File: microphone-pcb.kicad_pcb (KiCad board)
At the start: 4 copper layers, 10.7 x 11 mm, 13 parts, among them J1 Conn_FFC_Molex_5019510550

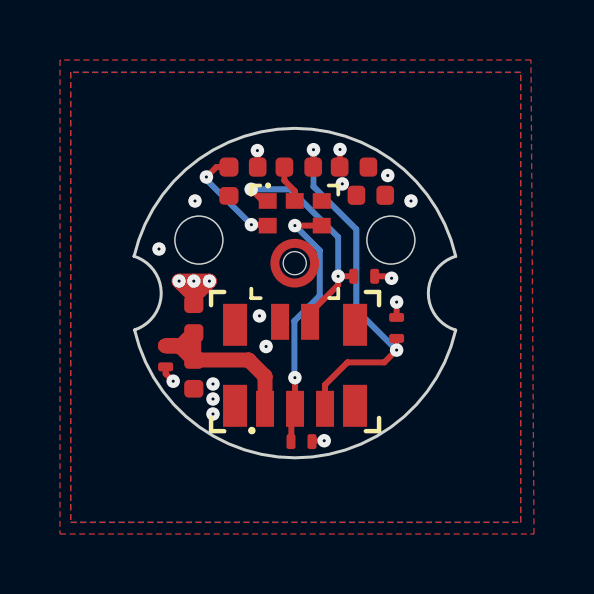
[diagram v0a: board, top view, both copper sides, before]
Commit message: [#71986] Update zones clearance
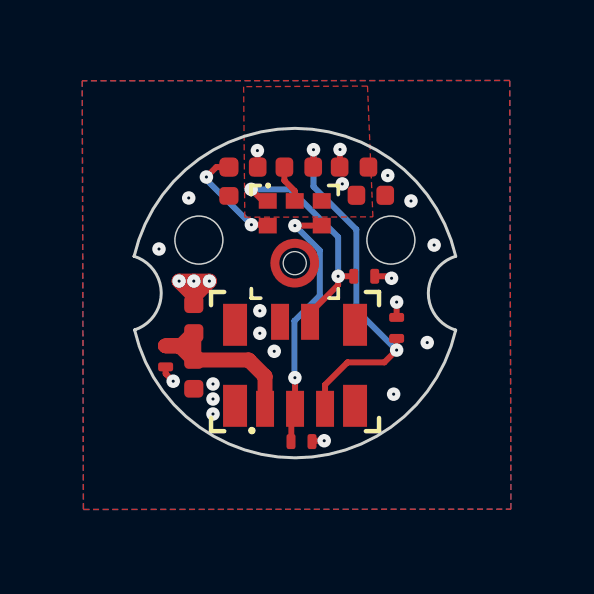
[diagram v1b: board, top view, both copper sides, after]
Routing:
- net GND: vias 13 -> 17
- added copper zone on In2.Cu, net GND

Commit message: [#71986] Update Silk L/R channels
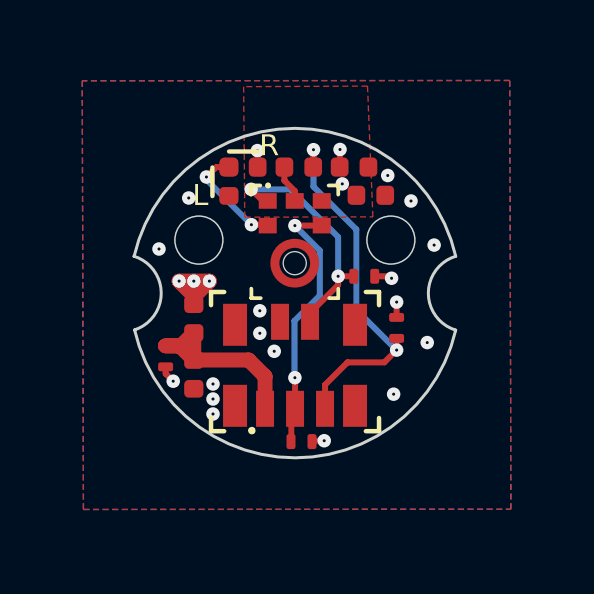
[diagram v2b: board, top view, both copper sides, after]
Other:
- board text added: "L"
- board text added: "R"
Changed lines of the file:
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@@
+	)
+	(gr_line
+		(start 238.7312 142.1966)
+		(end 237.7812 142.1966)
+		(stroke
+			(width 0.15)
+			(type default)
+		)
+		(layer "F.SilkS")
+	)
+	(gr_line
+		(start 237.2262 142.7316)
+		(end 237.2262 143.6816)
+		(stroke
+			(width 0.15)
+			(type default)
+		)
+		(layer "F.SilkS")
 	)
 	(gr_line
@@
 	)
 	(gr_text "Audio\nMicrophone\nRev. ${REVISION}"
-		(at 239.955108 151.027305 0)
+		(at 239.9462 151.5266 0)
 		(layer "B.SilkS")
 		(effects
@@
 	)
 	(gr_text "SHA:########"
-		(at 239.965108 147.637305 0)
+		(at 239.9562 148.1366 0)
 		(layer "B.SilkS")
 		(effects
@@
 		)
 	)
+	(gr_text "L"
+		(at 236.5562 144.0666 -0)
+		(layer "F.SilkS")
+		(effects
+			(font
+				(size 0.7 0.7)
+				(thickness 0.15)
+			)
+			(justify left bottom)
+		)
+	)
+	(gr_text "R\n"
+		(at 238.7862 142.4066 -0)
+		(layer "F.SilkS")
+		(effects
+			(font
+				(size 0.7 0.7)
+				(thickness 0.15)
+			)
+			(justify left bottom)
+		)
+	)

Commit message: [#71986] Update Rule for inner layers 0.4 mm clearance copper to edge
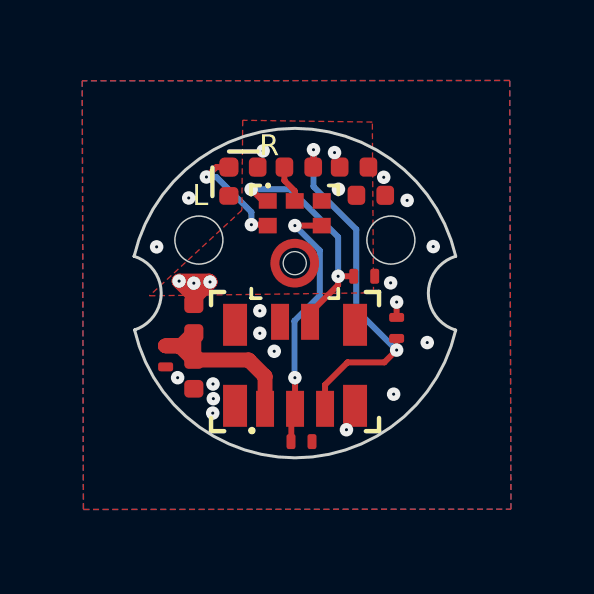
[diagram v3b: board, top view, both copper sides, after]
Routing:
- net GND: track 2.10 -> 0.62 mm
- net VDD: track 4.88 -> 3.68 mm
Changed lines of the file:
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@@
 	)
 	(segment
-		(start 236.605108 147.287305)
-		(end 236.605108 147.037305)
-		(width 0.5)
-		(layer "F.Cu")
-		(net 1)
-	)
-	(segment
-		(start 238.725108 142.167305)
-		(end 238.735108 142.177305)
-		(width 0.2)
-		(layer "F.Cu")
-		(net 1)
-	)
-	(segment
-		(start 236.605108 147.037305)
-		(end 237.125108 146.517305)
-		(width 0.5)
-		(layer "F.Cu")
-		(net 1)
-	)
-	(segment
-		(start 236.605108 147.287305)
-		(end 236.605108 146.517305)
+		(start 237.116905 146.517305)
+		(end 237.1462 146.5466)
 		(width 0.5)
 		(layer "F.Cu")
@@
 	(segment
 		(start 236.115108 146.517305)
-		(end 237.125108 146.517305)
-		(width 0.5)
-		(layer "F.Cu")
-		(net 1)
-	)
-	(segment
-		(start 241.478839 142.130061)
-		(end 241.475108 142.133792)
-		(width 0.2)
-		(layer "F.Cu")
-		(net 1)
-	)
-	(segment
-		(start 241.475108 142.133792)
-		(end 241.475108 142.717305)
-		(width 0.2)
-		(layer "F.Cu")
-		(net 1)
-	)
-	(segment
-		(start 238.735108 142.177305)
-		(end 238.735108 142.717305)
-		(width 0.2)
+		(end 237.116905 146.517305)
+		(width 0.5)
+		(layer "F.Cu")
+		(net 1)
+	)
+	(segment
+		(start 236.605108 147.087692)
+		(end 236.605108 147.287305)
+		(width 0.5)
+		(layer "F.Cu")
+		(net 1)
+	)
+	(segment
+		(start 237.1462 146.5466)
+		(end 236.605108 147.087692)
+		(width 0.5)
 		(layer "F.Cu")
 		(net 1)
@@
 	)
 	(segment
+		(start 236.605108 147.287305)
+		(end 236.605108 146.587692)
+		(width 0.5)
+		(layer "F.Cu")
+		(net 1)
+	)
+	(segment
 		(start 236.605108 147.007305)
 		(end 236.115108 146.517305)
@@
 		(net 1)
 	)
-	(via
-		(at 237.125108 146.517305)
+	(segment
+		(start 236.605108 146.587692)
+		(end 236.6062 146.5866)
+		(width 0.5)
+		(layer "F.Cu")
+		(net 1)
+	)
+	(via
+		(at 237.1462 146.5466)
 		(size 0.45)
 		(drill 0.1)
@@
 	)
 	(via
-		(at 236.605108 146.517305)
-		(size 0.45)
-		(drill 0.1)
-		(layers "F.Cu" "B.Cu")
-		(net 1)
-	)
-	(via
-		(at 241.478839 142.130061)
-		(size 0.45)
-		(drill 0.1)
-		(layers "F.Cu" "B.Cu")
-		(net 1)
-	)
-	(via
-		(at 241.555108 143.277305)
-		(size 0.45)
-		(drill 0.1)
-		(layers "F.Cu" "B.Cu")
-		(net 1)
-	)
-	(via
-		(at 238.725108 142.167305)
-		(size 0.45)
-		(drill 0.1)
-		(layers "F.Cu" "B.Cu")
-		(net 1)
-	)
-	(segment
-		(start 235.6662 149.601625)
-		(end 235.919037 149.854462)
-		(width 0.2)
-		(layer "F.Cu")
-		(net 2)
-	)
-	(segment
-		(start 240.604357 151.838443)
-		(end 240.952263 151.838443)
+		(at 241.296353 142.23374)
+		(size 0.45)
+		(drill 0.1)
+		(layers "F.Cu" "B.Cu")
+		(net 1)
+	)
+	(via
+		(at 236.6062 146.5866)
+		(size 0.45)
+		(drill 0.1)
+		(layers "F.Cu" "B.Cu")
+		(net 1)
+	)
+	(via
+		(at 241.426533 143.456267)
+		(size 0.45)
+		(drill 0.1)
+		(layers "F.Cu" "B.Cu")
+		(net 1)
+	)
+	(via
+		(at 238.9162 142.1766)
+		(size 0.45)
+		(drill 0.1)
+		(layers "F.Cu" "B.Cu")
+		(net 1)
+	)
+	(segment
+		(start 236.02551 149.6966)
+		(end 235.9872 149.6966)
 		(width 0.2)
 		(layer "F.Cu")
@@
 	)
 	(segment
-		(start 240.5562 151.8866)
-		(end 240.604357 151.838443)
-		(width 0.2)
-		(layer "F.Cu")
-		(net 2)
-	)
-	(segment
-		(start 243.131558 146.3566)
-		(end 243.197443 146.422485)
-		(width 0.2)
-		(layer "F.Cu")
-		(net 2)
-	)
-	(segment
 		(start 235.6662 149.3756)
-		(end 235.6662 149.601625)
-		(width 0.2)
-		(layer "F.Cu")
-		(net 2)
-	)
-	(segment
-		(start 242.6352 146.3566)
-		(end 243.131558 146.3566)
+		(end 235.6752 149.3756)
+		(width 0.2)
+		(layer "F.Cu")
+		(net 2)
+	)
+	(segment
+		(start 236.066191 149.737281)
+		(end 236.02551 149.6966)
 		(width 0.2)
 		(layer "F.Cu")
@@
 	)
 	(via
-		(at 237.245108 150.447305)
+		(at 237.2562 150.4366)
 		(size 0.45)
 		(drill 0.1)
@@
 	)
 	(via
-		(at 235.445108 145.447305)
-		(size 0.45)
-		(drill 0.1)
-		(layers "F.Cu" "B.Cu")
-		(free yes)
-		(net 2)
-	)
-	(via
-		(at 235.919037 149.854462)
-		(size 0.45)
-		(drill 0.1)
-		(layers "F.Cu" "B.Cu")
-		(net 2)
-	)
-	(via
-		(at 244.6162 145.3166)
-		(size 0.45)
-		(drill 0.1)
-		(layers "F.Cu" "B.Cu")
-		(net 2)
-	)
-	(via
-		(at 243.070108 142.997305)
+		(at 235.3662 145.3766)
+		(size 0.45)
+		(drill 0.1)
+		(layers "F.Cu" "B.Cu")
+		(free yes)
+		(net 2)
+	)
+	(via
+		(at 236.066191 149.737281)
+		(size 0.45)
+		(drill 0.1)
+		(layers "F.Cu" "B.Cu")
+		(net 2)
+	)
+	(via
+		(at 244.5862 145.3666)
+		(size 0.45)
+		(drill 0.1)
+		(layers "F.Cu" "B.Cu")
+		(net 2)
+	)
+	(via
+		(at 242.9362 143.0566)
 		(size 0.45)
 		(drill 0.1)
@@
 	)
 	(via
-		(at 243.845108 143.847305)
+		(at 243.7162 143.8266)
 		(size 0.45)
 		(drill 0.1)
@@
 	)
 	(via
-		(at 237.245108 150.947305)
+		(at 237.2362 150.9166)
 		(size 0.45)
 		(drill 0.1)
@@
 	)
 	(via
-		(at 243.197443 146.422485)
-		(size 0.45)
-		(drill 0.1)
-		(layers "F.Cu" "B.Cu")
-		(net 2)
-	)
-	(via
-		(at 240.952263 151.838443)
+		(at 243.1662 146.5766)
+		(size 0.45)
+		(drill 0.1)
+		(layers "F.Cu" "B.Cu")
+		(net 2)
+	)
+	(via
+		(at 241.693766 151.472076)
 		(size 0.45)
 		(drill 0.1)
@@
 	)
 	(segment
-		(start 237.025108 143.137305)
+		(start 238.525108 144.215508)
+		(end 237.356905 143.047305)
+		(width 0.2)
+		(layer "B.Cu")
+		(net 7)
+	)
+	(segment
+		(start 237.356905 143.047305)
 		(end 237.025108 143.047305)
 		(width 0.2)
@@
 	(segment
 		(start 238.525108 144.637305)
-		(end 237.025108 143.137305)
+		(end 238.525108 144.215508)
 		(width 0.2)
 		(layer "B.Cu")
@@
 	)
 	(zone
-		(net 1)
-		(net_name "VDD")
-		(layer "F.Cu")
+		(net 2)
+		(net_name "GND")
+		(layers "F.Cu" "In1.Cu" "In2.Cu" "B.Cu")
 		(hatch edge 0.5)
 		(connect_pads yes
-			(clearance 0.25)
+			(clearance 0.2)
 		)
-		(min_thickness 0.25)
-		(filled_areas_thickness no)
-		(fill yes
-			(thermal_gap 0.5)
-			(thermal_bridge_width 0.5)
-		)
-		(polygon
-			(pts
-				(xy 238.2662 140.0366) (xy 238.305108 144.3866) (xy 242.575108 144.3766) (xy 242.395108 140.0166)
-			)
-		)
-	)
-	(zone
-		(net 2)
-		(net_name "GND")
-		(layers "F&B.Cu")
-		(hatch edge 0.5)
-		(connect_pads yes
-			(clearance 0.25)
-		)
-		(min_thickness 0.25)
+		(min_thickness 0.2)
 		(filled_areas_thickness no)
 		(fill yes
@@
 	)
 	(zone
-		(net 2)
-		(net_name "GND")
-		(layers "In1.Cu" "In2.Cu")
+		(net 1)
+		(net_name "VDD")
+		(layers "F.Cu" "In2.Cu")
 		(hatch edge 0.5)
+		(priority 1)
 		(connect_pads yes
-			(clearance 0.4)
+			(clearance 0.2)
 		)
-		(min_thickness 0.25)
+		(min_thickness 0.2)
 		(filled_areas_thickness no)
 		(fill yes
@@
 		(polygon
 			(pts
-				(xy 232.5 139.56) (xy 232.5 154.56) (xy 247.5 154.56) (xy 247.5 139.56)
+				(xy 238.2362 141.1566) (xy 238.2062 144.1566) (xy 235.125108 147.007305) (xy 242.595108 146.907305)
+				(xy 242.5562 141.2166)
 			)
 		)
-	)
-	(zone
-		(net 1)
-		(net_name "VDD")
-		(layer "In2.Cu")
-		(hatch edge 0.5)
-		(priority 1)
-		(connect_pads yes
-			(clearance 0.4)
-		)
-		(min_thickness 0.25)
-		(filled_areas_thickness no)
-		(fill yes
-			(thermal_gap 0.5)
-			(thermal_bridge_width 0.5)
-		)
-		(polygon
-			(pts
-				(xy 232.145108 139.147305) (xy 232.115108 146.977305) (xy 247.915108 146.977305) (xy 247.845108 139.147305)
-			)
-		)
